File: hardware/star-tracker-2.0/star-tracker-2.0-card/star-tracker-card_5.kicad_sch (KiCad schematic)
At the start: 33 parts, among them Q1 MMBT2907, U10 TLVH431, U4 SN74LVC1G07DCK, U7 OSD3358-512M-BSM

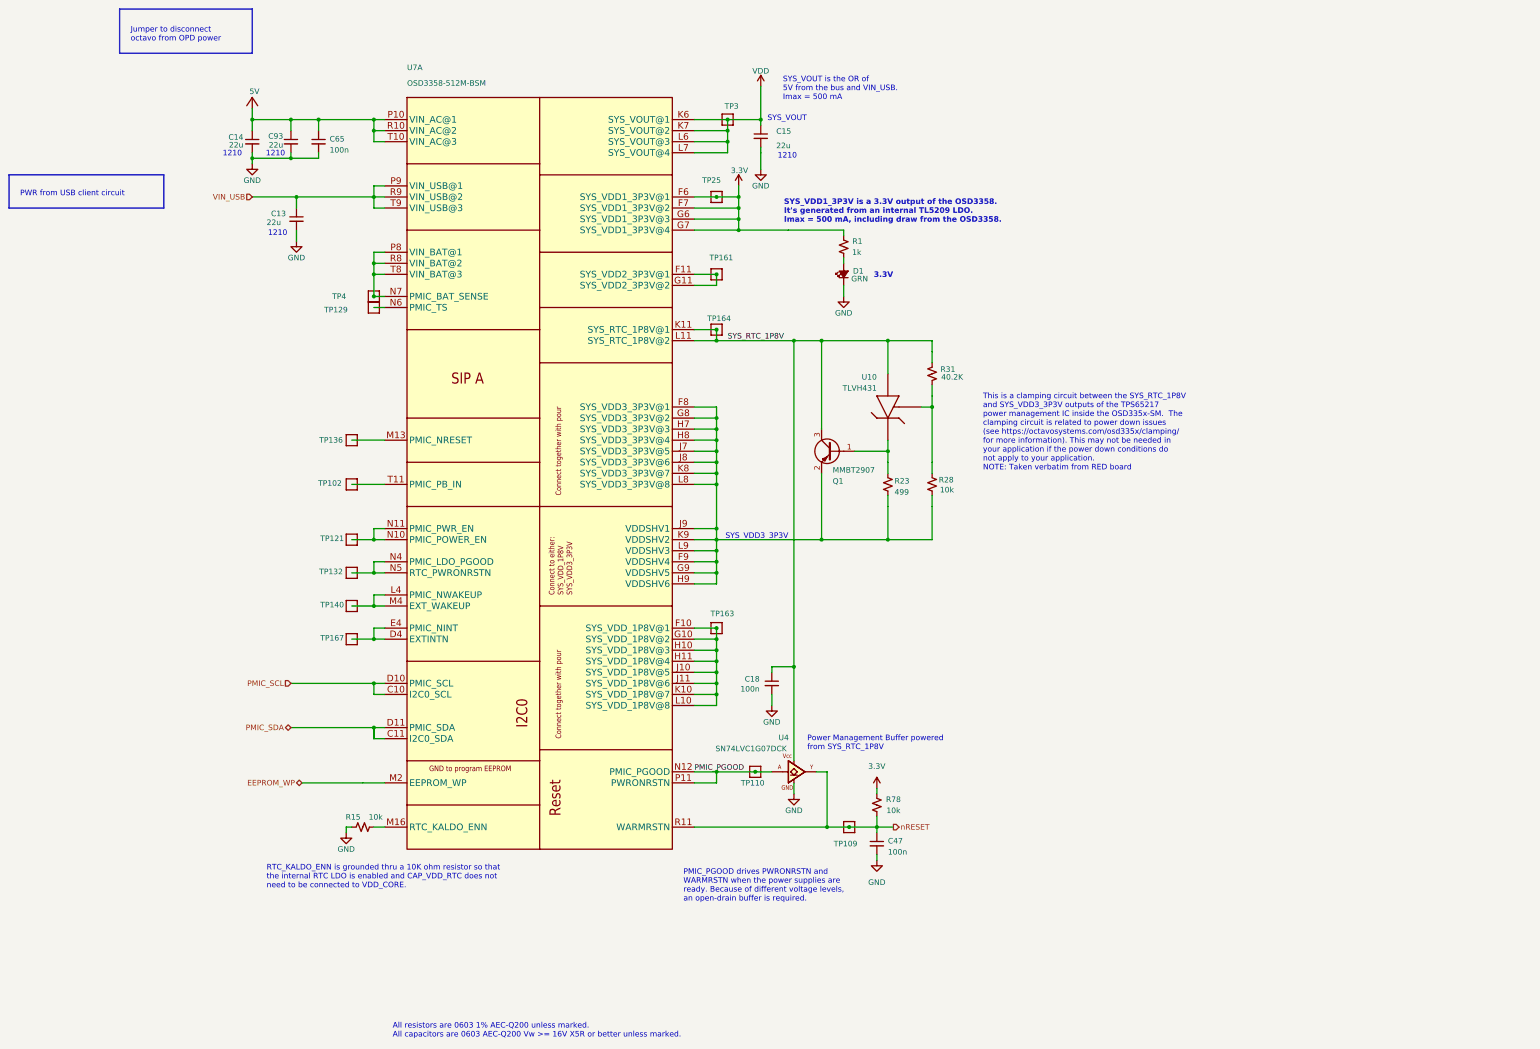
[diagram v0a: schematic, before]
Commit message: Added IMU
added IMU, and i2c pull up resistors to schematic.
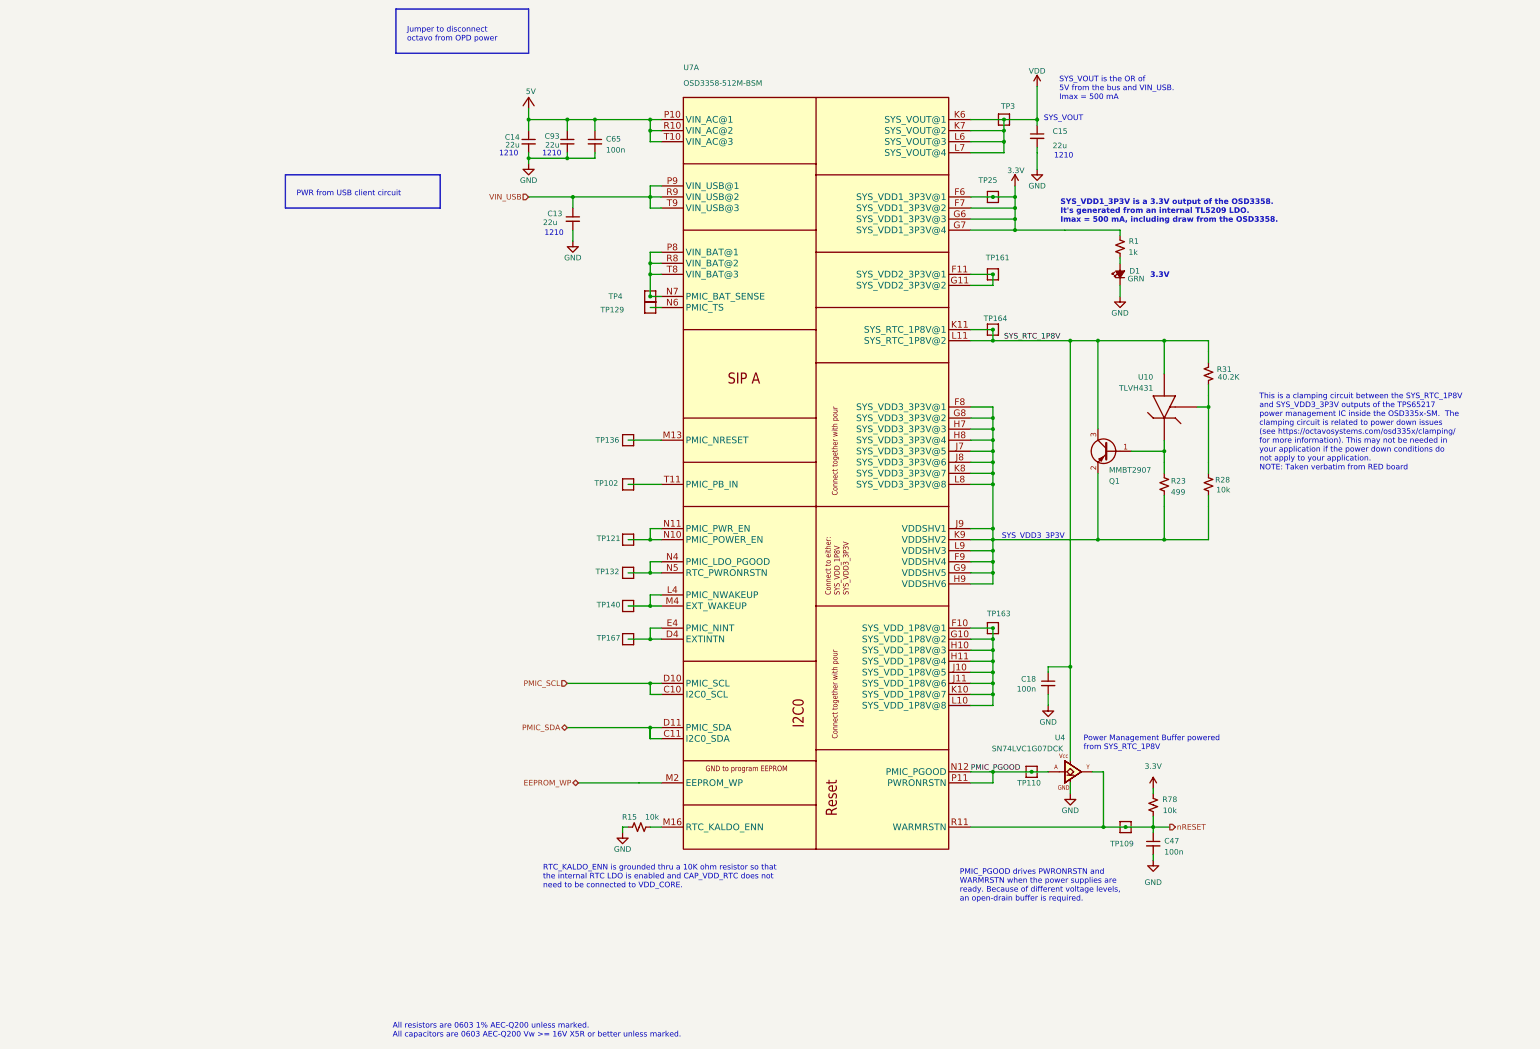
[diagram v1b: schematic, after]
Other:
- moved on the sheet: C13, C14, C15, C18, C47, C65, C93, D1, Q1, R1, R15, R23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

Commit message: Routine Push
Updated schematic and layout. about 60% done with routing.
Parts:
- removed TP102, TP121, TP129, TP132, TP136, TP140, TP161, TP163, TP164, TP167, TP25, TP4: TEST-POINT3X4, oresat-misc:TestPoint_Pad_D1.0mm, symbol oresat-misc:Test-Point-1mm-round
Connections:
- no-connect marks 0 -> 3

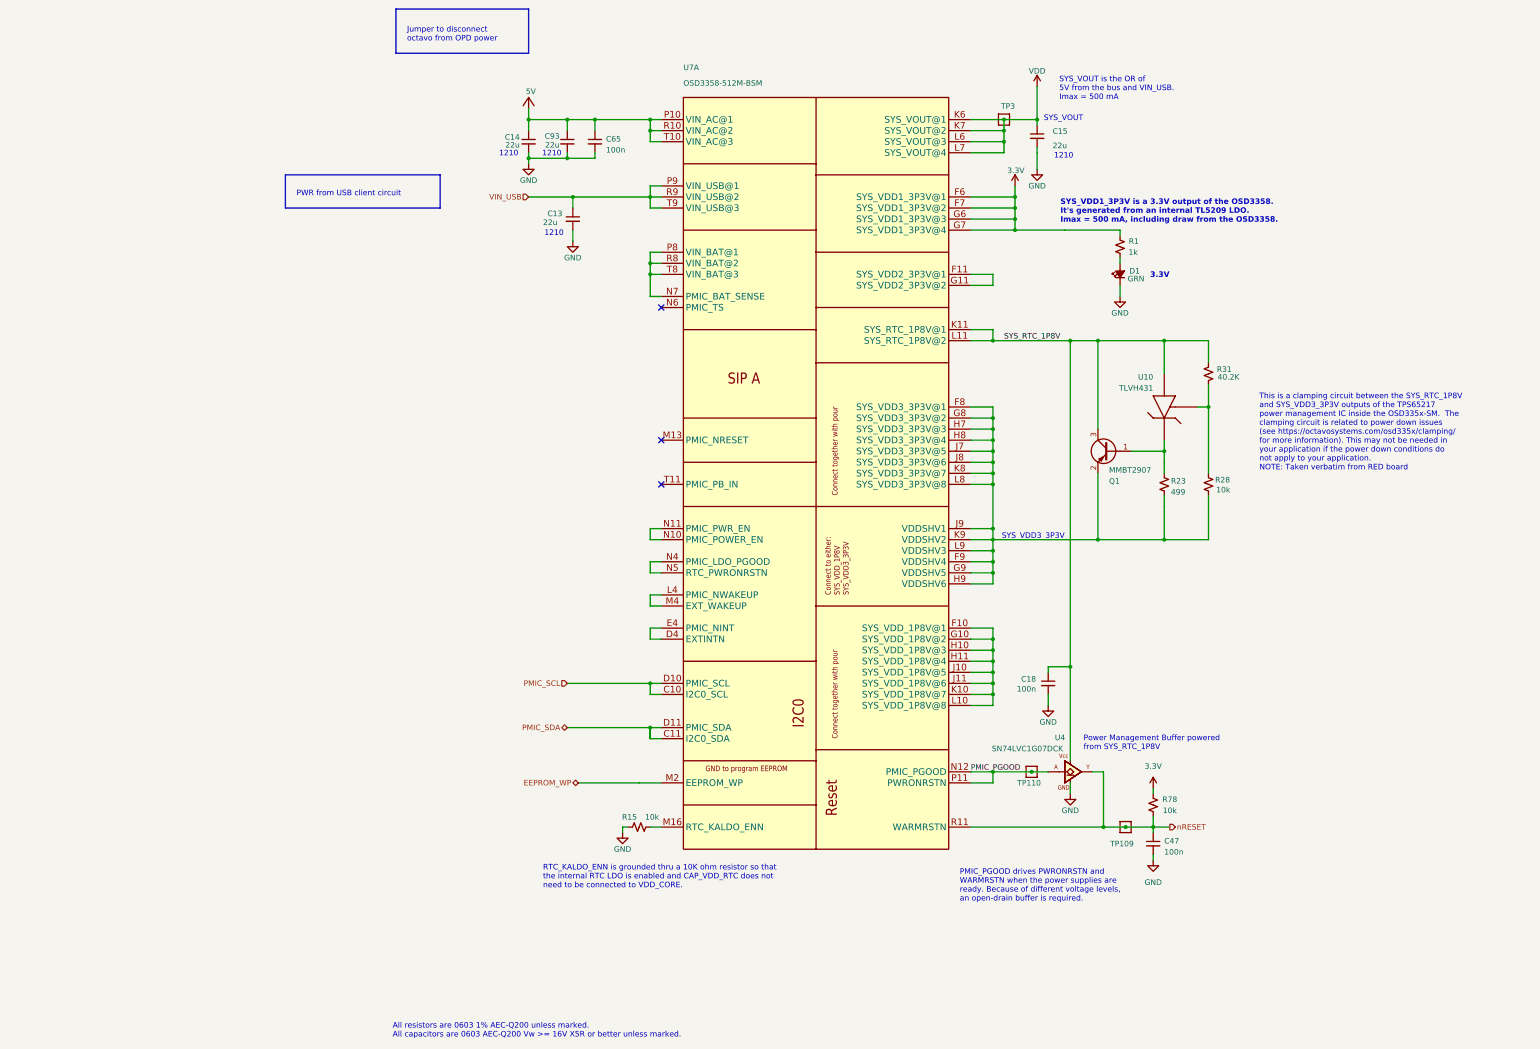
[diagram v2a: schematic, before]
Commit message: Star tracker board update
Added 3d models to footprints, reannotated component designators
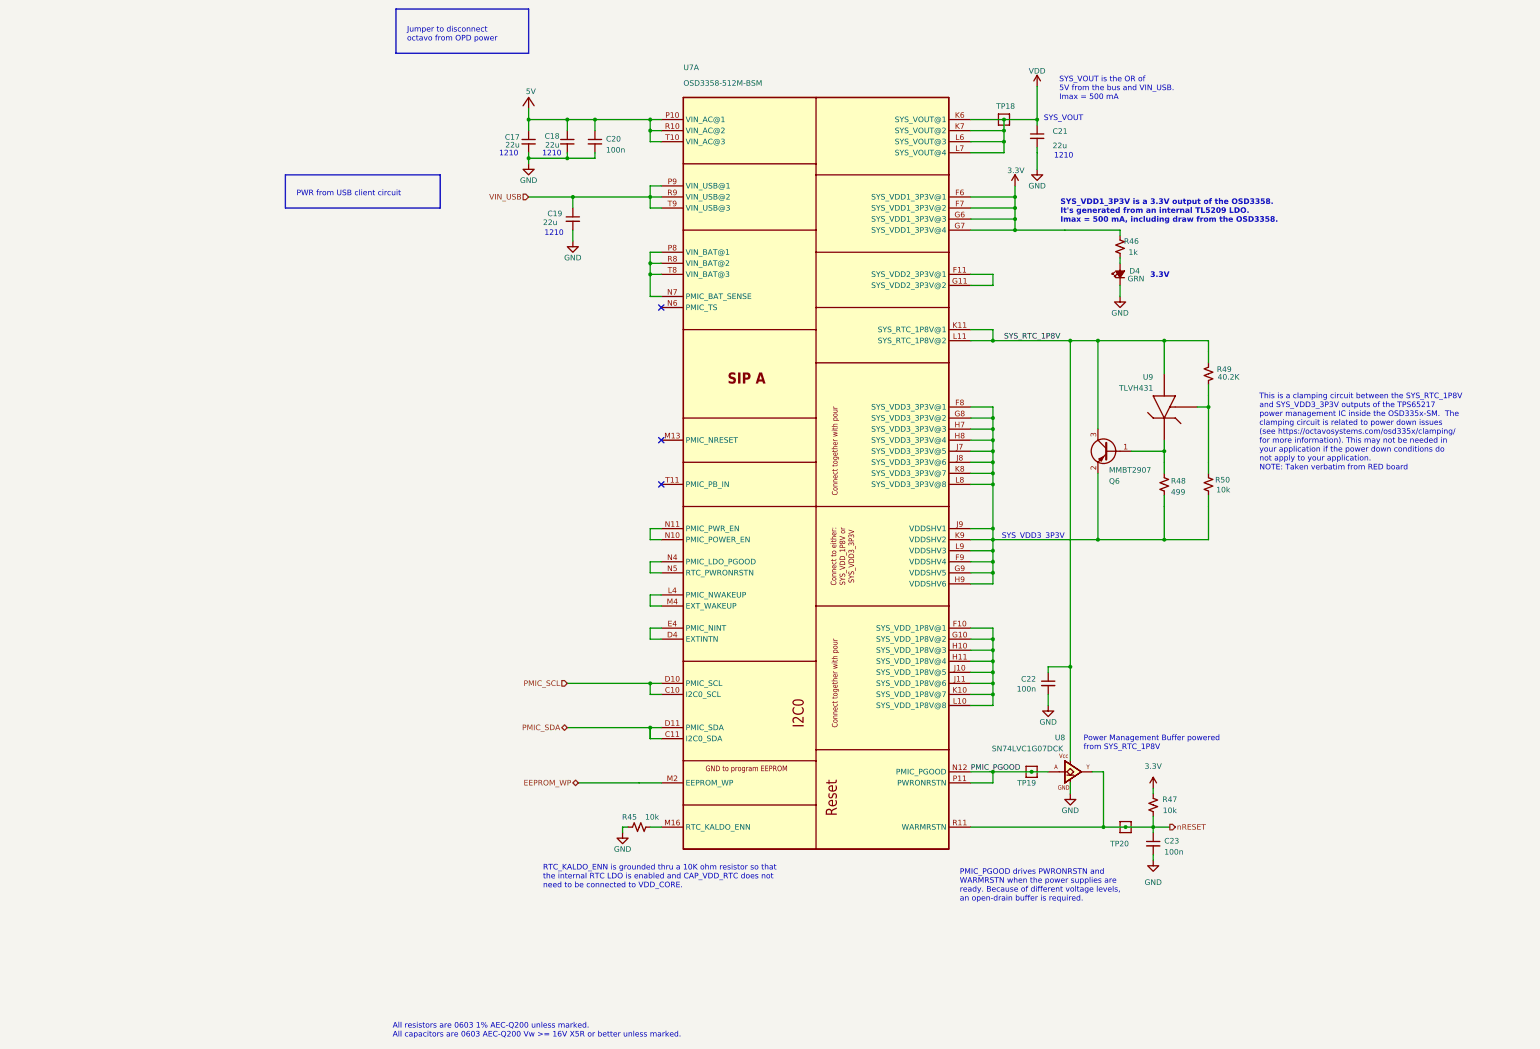
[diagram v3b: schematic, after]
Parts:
- U7: footprint star-tracker-card:OSD335X-BGA-256 -> oresat-ics:U-Octavo-OSD335X-BGA-256; symbol star-tracker-card-eagle-import:OSD3358-512M-BSM -> oresat-ics:OSD3358-512M-BSM; Distributor (none) -> DigiKey; MPN OSD3358-1G-ISM -> OSD3358-512M-BSM
- renumbered C14 to C17, C93 to C18, C13 to C19, C65 to C20, C15 to C21, C18 to C22, C47 to C23, D1 to D4, Q1 to Q6, R15 to R45, R1 to R46, R78 to R47, R23 to R48, R31 to R49, R28 to R50, TP3 to TP18, TP110 to TP19, TP109 to TP20, U4 to U8, U10 to U9

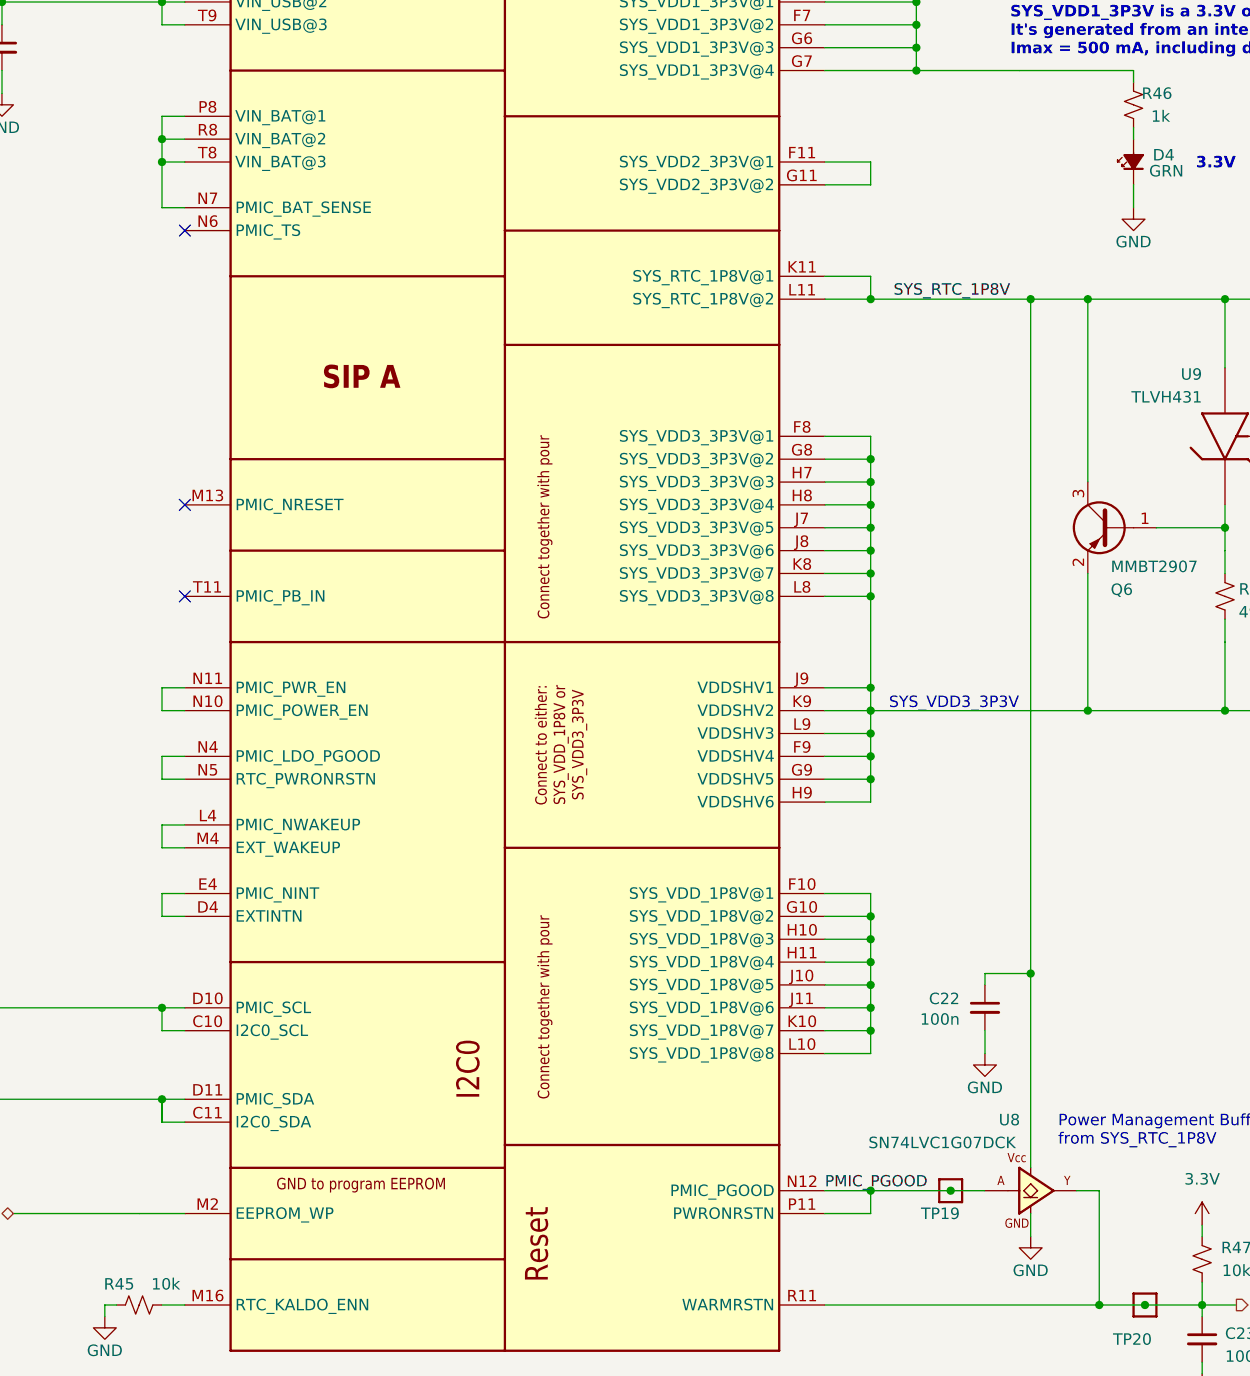
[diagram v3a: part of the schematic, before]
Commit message: Update to Camera Board
Update BOM for camera board, replaced lower tier dielectric caps to X7R
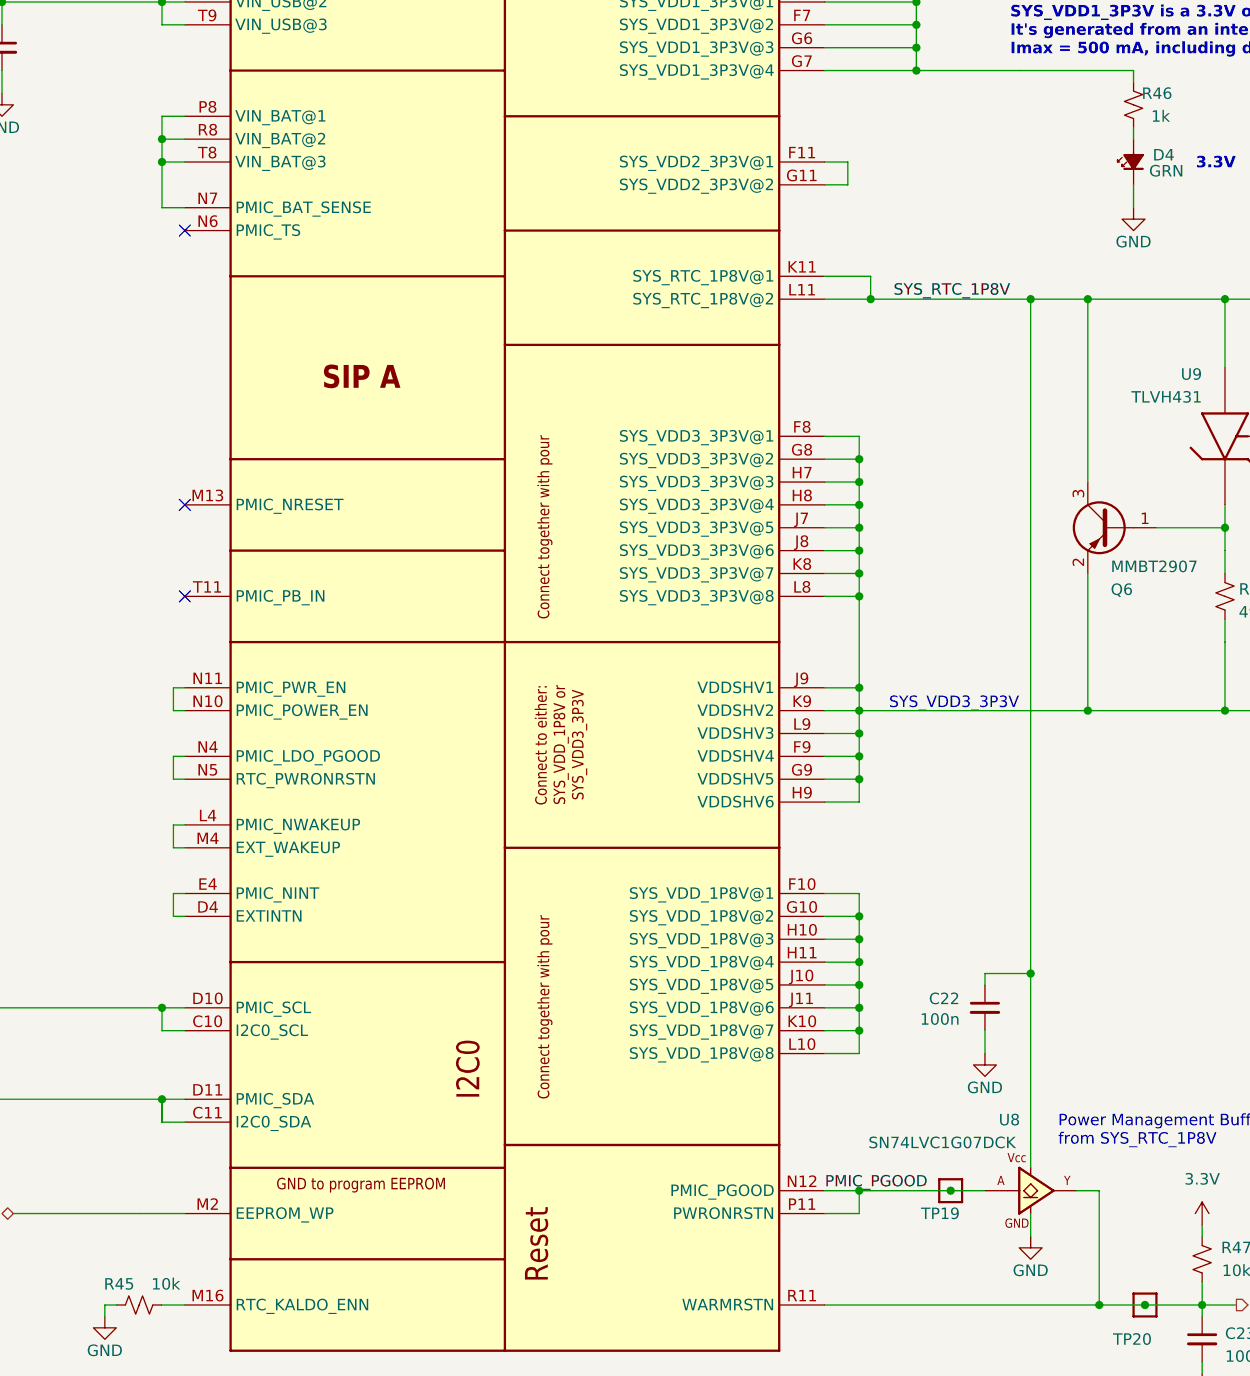
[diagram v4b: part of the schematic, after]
